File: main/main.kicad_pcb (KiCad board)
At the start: 6 copper layers, 154 parts, among them IC1 TPS54294PWP, IC2 TPS54294PWP, IC3 ESP-PSRAM64H, IC4 PCM1741E, J1 STX-3000, J2 DIN-5_180degree, J3 Barrel_Jack_Switch_Pin3Ring, J4 FPGA_debug, J5 FPGA_GPIO, J6 MCU_debug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

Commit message: Continue PCB layout
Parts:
- moved C66 219.2 mm to (240.8, 88.9), turned to 180 degrees
- moved U5 218.3 mm to (249.4, 91.3)
- moved R41 216.6 mm to (231.0, 88.9), turned to 180 degrees
- moved R40 215.9 mm to (235.7, 86.7)
- moved J1 215.1 mm to (248.4, 78.8)
- moved C67 214.2 mm to (225.2, 88.9), turned to 0 degrees
- moved R42 213.7 mm to (235.7, 88.9), turned to 180 degrees
- moved C68 213.5 mm to (231.0, 86.7), turned to 180 degrees
- moved C64 204.4 mm to (224.2, 80.5)
- moved C65 204.2 mm to (237.3, 80.5)
- moved IC4 204.2 mm to (229.9, 80.5)
- moved C69 199.9 mm to (240.8, 93.9)
- moved J3 193.8 mm to (45.2, 104.0), turned to 270 degrees
- moved C70 181.2 mm to (225.2, 93.8)
- moved C55 156.5 mm to (42.7, 172.8)
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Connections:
- JP2 pad 1: +1V8 -> Net-(C14-Pad1)
- JP2 pad 2: Net-(C14-Pad1) -> +1V8
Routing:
- net /DAC/LINE_OUT_R: track 0.00 -> 48.9 mm
- net Net-(C1-Pad1): track 0.00 -> 47.1 mm
- net /MCU/MIDI_IN: track 76.5 -> 43.8 mm
- net /MCU/FBKey4: track 12.1 -> 42.9 mm
- net /DAC/LINE_OUT_L: track 0.00 -> 30.0 mm, vias 0 -> 2
- net Net-(C65-Pad1): track 0.00 -> 26.5 mm
- net /MCU/FBKey3: track 14.0 -> 37.4 mm
- net Net-(C4-Pad1): track 3.13 -> 26.1 mm
- net Net-(C69-Pad2): track 0.00 -> 23.0 mm
- net Net-(R29-Pad1): track 0.00 -> 22.3 mm
- net /FBKey0: track 18.5 -> 38.4 mm
- net Net-(R28-Pad1): track 0.00 -> 19.4 mm
- net /FBKey2: track 14.7 -> 33.7 mm
- net /FBKey1: track 15.9 -> 34.5 mm
- net Net-(R27-Pad1): track 0.00 -> 16.5 mm
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
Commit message: Continue PCB layout
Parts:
- Backup SPI: renamed from J8
- I2S Breakout: renamed from J9
- moved R36 218.3 mm to (231.1, 31.2)
- moved I2S Breakout 189.7 mm to (229.0, 53.0)
- moved R35 169.4 mm to (206.1, 62.5)
- moved R33 168.6 mm to (206.1, 66.5)
- moved R31 167.8 mm to (206.1, 70.5)
- moved B 166.5 mm to (184.8, 79.8), turned to 0 degrees
- moved A 165.3 mm to (184.8, 75.6), turned to 0 degrees
- moved C 157.2 mm to (184.8, 84.0), turned to 0 degrees
- moved R39 156.4 mm to (191.4, 84.0)
- moved R37 150.6 mm to (191.4, 79.8)
- moved R38 142.0 mm to (191.4, 75.6)
- moved R19 98.6 mm to (291.9, 139.6)
- moved R24 94.4 mm to (288.9, 132.2)
- moved C30 92.7 mm to (286.0, 145.6)
- moved C40 89.9 mm to (283.0, 143.1)
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- renumbered R32 to A, R30 to B, R34 to C
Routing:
- net Net-(R34-Pad2): track 0.00 -> 35.5 mm, vias 0 -> 2
- net /DAC/I2S1: track 0.00 -> 32.0 mm, vias 0 -> 2
- net /DAC/I2S2: track 0.00 -> 28.9 mm
- net /DAC/I2S0: track 0.00 -> 26.0 mm
- net Net-(R32-Pad2): track 0.00 -> 24.0 mm
- net Net-(R30-Pad2): track 0.00 -> 23.9 mm, vias 0 -> 2
- net Net-(J9-Pad3): track 4.16 -> 27.4 mm
- net Net-(J9-Pad2): track 4.16 -> 26.7 mm
- net Net-(J9-Pad1): track 4.18 -> 26.1 mm
- net /DAC/DAC_I2S_LR_SELECT: track 0.00 -> 16.5 mm
- net /DAC/DAC_I2S_DATA: track 0.00 -> 14.3 mm
- net /DAC/DAC_I2S_CLK: track 0.00 -> 13.3 mm
- net Net-(C1-Pad1): track 47.1 -> 52.8 mm
- net Net-(D1-Pad2): track 59.0 -> 63.6 mm
- net Net-(D1-Pad1): track 19.9 -> 24.0 mm
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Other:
- copper layers 6 -> 4
- board text added: "Solder here and cut A, B and C to use breakout I2S"

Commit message: Some more routing
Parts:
- moved C30 127.9 mm to (195.0, 55.6)
- moved C40 126.8 mm to (180.0, 69.2), turned to 270 degrees
- moved C39 120.8 mm to (177.5, 69.2), turned to 270 degrees
- moved C28 118.5 mm to (195.0, 50.7)
- moved C44 115.0 mm to (190.0, 65.5), turned to 180 degrees
- moved C20 112.3 mm to (190.5, 40.0)
- moved C43 112.1 mm to (190.0, 63.4), turned to 180 degrees
- moved C27 108.9 mm to (195.0, 48.2)
- moved C21 107.8 mm to (190.2, 61.1), turned to 180 degrees
- moved C31 105.5 mm to (195.0, 58.1)
- moved C25 105.2 mm to (190.2, 50.8), turned to 180 degrees
- moved C34 103.4 mm to (195.0, 65.5)
- moved C26 100.2 mm to (190.2, 48.2), turned to 180 degrees
- moved C33 99.5 mm to (195.0, 63.0)
- moved C32 98.7 mm to (195.0, 60.6)
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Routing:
- net GND: track 0.00 -> 104.1 mm, vias 0 -> 5
- net +1V0: track 0.00 -> 88.1 mm, vias 0 -> 6
- net +1V8: track 0.00 -> 27.6 mm
- net +3V3: track 0.16 -> 19.9 mm
- net Net-(U2-Pad6): track 0.00 -> 7.87 mm
- added copper zone on In2.Cu, net +3V3
- added copper zone on In1.Cu, net GND
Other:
- board outline added: 292.1 x 177.8 mm

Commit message: PCB getting close to being fully connected
Still missing the power circuit, will look at it tomorrow.
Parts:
- removed A, B, C: 0, Jumper:SolderJumper-2_P1.3mm_Bridged2Bar_RoundedPad1.0x1.5mm
- added R30: 0, Jumper:SolderJumper-2_P1.3mm_Bridged2Bar_RoundedPad1.0x1.5mm, F.Cu at (224.5, 105.3)
- added R32: 0, Jumper:SolderJumper-2_P1.3mm_Bridged2Bar_RoundedPad1.0x1.5mm, F.Cu at (224.5, 101.1)
- added R34: 0, Jumper:SolderJumper-2_P1.3mm_Bridged2Bar_RoundedPad1.0x1.5mm, F.Cu at (224.5, 109.4)
- J8: renamed from Backup SPI
- J9: renamed from I2S Breakout
- moved R24 155.5 mm to (148.8, 64.8), turned to 270 degrees
- moved C48 137.3 mm to (171.4, 44.2), turned to 90 degrees
- moved C52 134.3 mm to (183.8, 44.4), turned to 90 degrees
- moved R23 133.0 mm to (154.9, 58.9), turned to 90 degrees
- moved J8 132.6 mm to (94.8, 21.3), turned to 270 degrees
- moved R21 129.5 mm to (177.4, 29.0), turned to 90 degrees
- moved R22 129.5 mm to (173.9, 29.1), turned to 90 degrees
- moved R25 127.0 mm to (152.9, 64.8), turned to 270 degrees
- moved C49 126.5 mm to (174.7, 44.4), turned to 90 degrees
- moved R19 123.1 mm to (179.8, 88.8)
- moved C51 122.6 mm to (180.7, 44.4), turned to 90 degrees
- moved C50 114.4 mm to (177.7, 44.4), turned to 90 degrees
- moved C53 112.2 mm to (186.8, 44.4), turned to 90 degrees
- moved C47 111.2 mm to (167.9, 44.2), turned to 90 degrees
- moved C46 100.2 mm to (173.1, 38.0), turned to 90 degrees
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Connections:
- J5 pad 1: /FPGA/GPIO0 -> +3V3
- J5 pad 10: /FPGA/GPIO5 -> /FPGA/GPIO4
- J5 pad 2: /FPGA/GPIO9 -> GND
- J5 pad 3: /FPGA/GPIO1 -> /FPGA/GPIO0
- J5 pad 4: /FPGA/GPIO8 -> /FPGA/GPIO7
- J5 pad 5: /FPGA/GPIO2 -> /FPGA/GPIO1
- J5 pad 6: /FPGA/GPIO7 -> /FPGA/GPIO6
- J5 pad 7: /FPGA/GPIO3 -> /FPGA/GPIO2
- J5 pad 8: /FPGA/GPIO6 -> /FPGA/GPIO5
- J5 pad 9: /FPGA/GPIO4 -> /FPGA/GPIO3
- L2 pad 1: Net-(C14-Pad1) -> Net-(C12-Pad2)
- L2 pad 2: Net-(C12-Pad2) -> Net-(C14-Pad1)
- U3 pad P8: /FPGA/GPIO9 -> Net-(U3-PadP8)
- U3 pad R5: /FPGA/GPIO3 -> /FPGA/GPIO0
- U3 pad R6: /FPGA/GPIO1 -> /FPGA/GPIO7
- U3 pad R7: /FPGA/GPIO0 -> Net-(U3-PadR7)
- U3 pad R8: /FPGA/GPIO8 -> Net-(U3-PadR8)
- U3 pad T12: Net-(U3-PadT12) -> /FPGA/GPIO3
- U3 pad T5: /FPGA/GPIO2 -> /FPGA/GPIO6
- U3 pad T7: /FPGA/GPIO7 -> /FPGA/GPIO1
- U3 pad T8: /FPGA/GPIO6 -> /FPGA/GPIO5
- U3 pad T9: /FPGA/GPIO5 -> /FPGA/GPIO2
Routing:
- net GND: track 104.1 -> 329.8 mm, vias 5 -> 26
- net +3V3: track 19.9 -> 184.2 mm, vias 0 -> 13
- net /MCU/~RESET: track 0.00 -> 96.6 mm, vias 0 -> 1
- net /MCU/BACKUP_SPI_CLK: track 0.00 -> 93.8 mm, vias 0 -> 1
- net /MCU/BACKUP_SPI_MISO: track 0.00 -> 93.4 mm, vias 0 -> 1
- net /MCU/BACKUP_SPI_MOSI: track 0.00 -> 93.3 mm, vias 0 -> 1
- net /MCU/BACKUP_SPI_CS: track 0.00 -> 92.6 mm, vias 0 -> 1
- net /MCU/GPIO9: track 0.00 -> 91.2 mm, vias 0 -> 2
- net /MCU/GPIO8: track 0.00 -> 85.5 mm, vias 0 -> 2
- net /MCU/GPIO7: track 0.00 -> 75.7 mm
- net /MCU/GPIO0: track 0.00 -> 74.9 mm
- net /MCU/GPIO1: track 0.00 -> 71.3 mm
- net /MCU/GPIO6: track 0.00 -> 70.8 mm
- net /MCU/DBG_SWDIOTMS: track 0.00 -> 70.0 mm, vias 0 -> 1
- net /MCU/GPIO2: track 0.00 -> 69.2 mm
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
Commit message: Almost finished with PCB layout
- Fixed FPGA power layout. The 1V0, 1V8 and 3V3 pins have to be
  connected to vias which in turn connect to fat lanes

- Added logo and names

- Started power circuit, this needs some work
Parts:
- added logo: G***, logo:logo, F.Cu at (72.8, 97.2)
- added svg2mod: G***, logo:logo, F.Cu at (207.0, 67.6)
- moved C6 200.4 mm to (213.5, 58.6), turned to 90 degrees
- moved R13 188.6 mm to (205.0, 55.1), turned to 180 degrees
- moved L3 188.5 mm to (208.4, 99.6), turned to 270 degrees
- moved C14 183.4 mm to (205.0, 58.7), turned to 180 degrees
- moved C15 178.1 mm to (205.0, 62.3), turned to 180 degrees
- moved L2 175.8 mm to (208.4, 62.5), turned to 90 degrees
- moved J3 175.7 mm to (217.0, 67.4), turned to 90 degrees
- moved C8 174.3 mm to (206.5, 67.2), turned to 180 degrees
- moved C9 170.1 mm to (206.5, 70.5), turned to 180 degrees
- moved R16 168.7 mm to (200.2, 55.1), turned to 180 degrees
- moved C12 164.9 mm to (205.8, 74.8), turned to 90 degrees
- moved C13 164.7 mm to (205.8, 87.3), turned to 270 degrees
- moved C11 164.5 mm to (206.5, 95.0), turned to 180 degrees
- moved C16 164.4 mm to (205.2, 100.0), turned to 180 degrees
- moved C17 164.4 mm to (205.2, 103.5), turned to 180 degrees
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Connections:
- net Net-(C1-Pad1) renamed /Power Supply/POWER_IN
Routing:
- net +3V3: track 184.2 -> 403.0 mm, vias 13 -> 24
- net /DAC/DAC_MODE_LATCH: track 0.00 -> 113.2 mm, vias 0 -> 2
- net /DAC/DAC_MODE_DATA: track 0.00 -> 110.0 mm, vias 0 -> 2
- net /DAC/DAC_MODE_CTRL_CLK: track 0.00 -> 109.7 mm, vias 0 -> 2
- net /FPGA/MCU_CLOCK_IN: track 4.04 -> 85.4 mm, vias 0 -> 2
- net +3.3VA: track 0.00 -> 75.6 mm
- net /DAC/DAC_SYS_CLK: track 1.03 -> 76.4 mm, vias 0 -> 2
- net Net-(C14-Pad1): track 12.7 -> 84.7 mm
- net /DAC/I2S0: track 1.06 -> 53.7 mm, vias 0 -> 2
- net /DAC/I2S2: track 7.18 -> 59.3 mm, vias 0 -> 2
- net /DAC/I2S1: track 1.12 -> 51.5 mm, vias 0 -> 2
- net /FBKey0: track 38.4 -> 83.3 mm
- net GND: track 329.8 -> 373.4 mm, vias 26 -> 94
- net /MCU/FPGA_PROGRAM_B: track 7.34 -> 49.7 mm, vias 0 -> 2
- net /FPGA/DONE: track 10.8 -> 52.4 mm, vias 0 -> 2
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- added copper zone on F.Cu, net /Power Supply/POWER_IN
- added copper zone on F.Cu, net GND
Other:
- board size 292.1 x 177.8 mm -> 166.6 x 111.3 mm
- net class Default: clearance 0.2 -> 0.15; via_dia 0.8 -> 0.6; via_drill 0.4 -> 0.3
- net class Power added: clearance 0.15, trace_width 0.6, via_dia 0.6, via_drill 0.3
- rule trace_clearance: 0.2 -> 0.15
- board text added: "Andreas Klavenes Berg Eivind Kløvjan Halvor Bjørstad Iver Håkonsen Lars Murud Aurud Magnus Alexander Krumbacher Oskar Sveinsen"

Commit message: Finished (?) board
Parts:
- moved D2 50.2 mm to (184.6, 146.6)
- moved FB1 50.2 mm to (176.1, 151.3)
- moved R11 50.2 mm to (176.1, 146.6)
- moved R12 50.2 mm to (184.8, 151.3)
- moved R10 39.2 mm to (210.0, 85.5), turned to 180 degrees
- moved R17 33.9 mm to (192.6, 86.7), turned to 270 degrees
- moved JP3 15.0 mm to (184.5, 121.7), turned to 180 degrees
- moved JP1 5.37 mm to (184.5, 107.3), turned to 180 degrees
- moved JP2 4.82 mm to (184.5, 114.5), turned to 180 degrees
- moved C20 1.70 mm to (178.9, 69.4)
- moved C42 1.70 mm to (181.0, 75.0)
- moved C18 0.56 mm to (199.7, 87.7)
- moved C43 0.45 mm to (179.0, 95.0)
- moved C44 0.45 mm to (179.0, 97.1)
- moved R15 0.19 mm to (200.1, 107.2)
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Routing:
- net +1V0: track 126.6 -> 51.1 mm
- net +1V8: track 76.7 -> 57.8 mm
- net +3V3: track 403.0 -> 385.8 mm, vias 24 -> 25
- net +3.3VA: track 75.6 -> 90.6 mm
- net Net-(C16-Pad1): track 24.4 -> 38.5 mm
- net Net-(C18-Pad1): track 0.00 -> 12.1 mm, vias 0 -> 2
- net Net-(J9-Pad1): track 34.3 -> 22.6 mm
- net Net-(C14-Pad1): track 84.7 -> 96.0 mm
- net Net-(IC2-Pad12): track 17.5 -> 28.0 mm, vias 2 -> 3
- net Net-(C7-Pad1): track 3.37 -> 11.4 mm, vias 0 -> 2
- net Net-(J9-Pad2): track 29.5 -> 23.1 mm
- net Net-(C4-Pad1): track 61.5 -> 55.5 mm
- net Net-(IC1-Pad11): track 29.1 -> 34.2 mm
- net GND: track 373.4 -> 368.5 mm, vias 94 -> 95
- net Net-(J9-Pad3): track 24.9 -> 23.7 mm
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- added copper zone on F.Cu, net +1V0
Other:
- board size 166.6 x 111.3 mm -> 166 x 112 mm
- board text added: "Debug"
- board text added: "FPGA"
- board text added: "GPIO"
- board text added: "MCU"
- board text added: "SPI"
- board text removed: "Solder here and cut A, B and C to use breakout I2S"

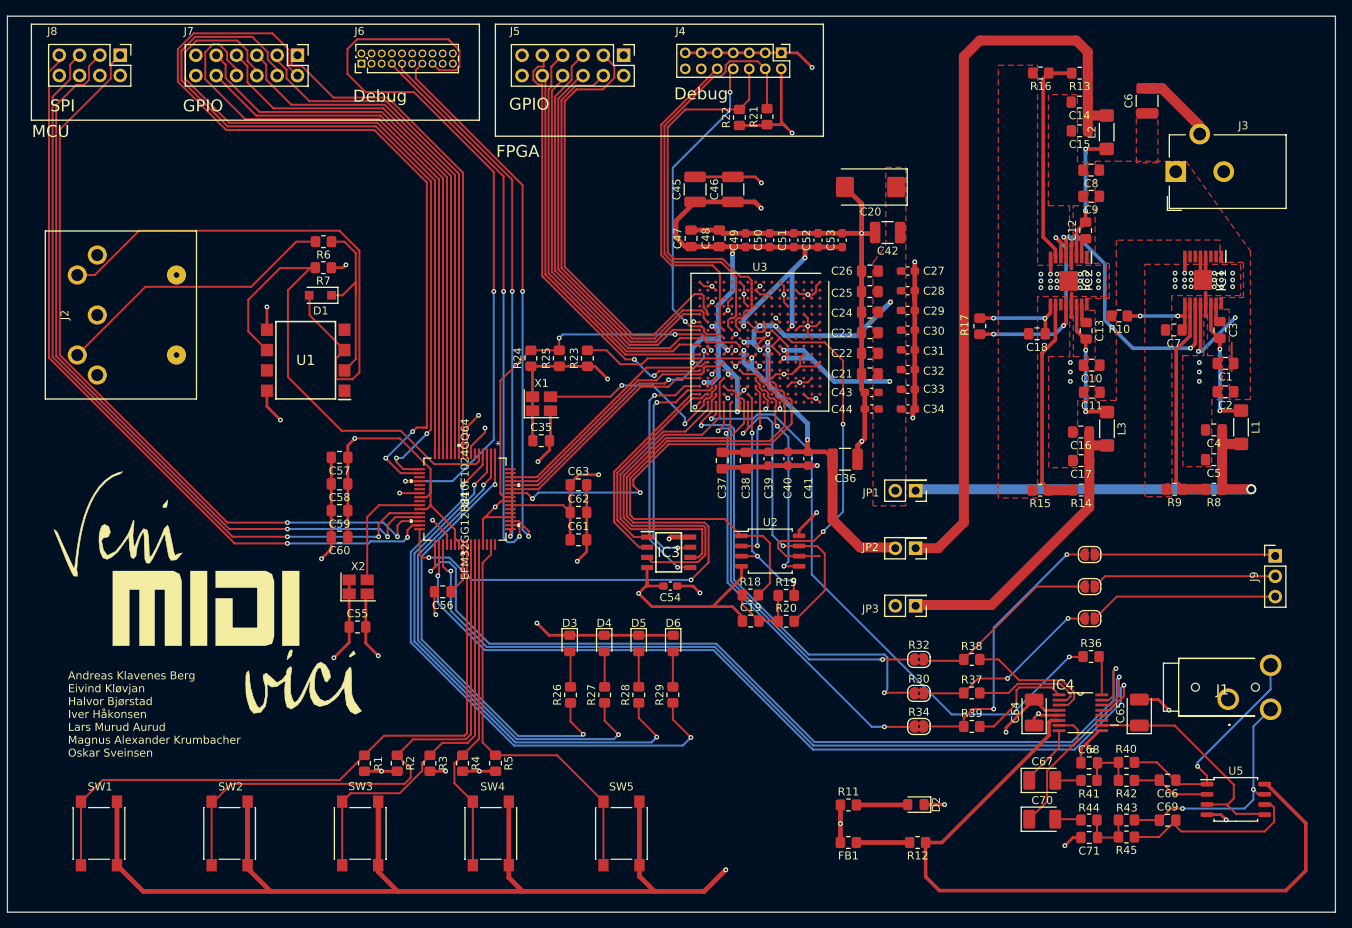
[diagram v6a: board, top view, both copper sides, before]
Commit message: Fixes after review
- +1V0 and +1V8 power zones on the backside of the FPGA
- Vias directly next to decoupling capacitors
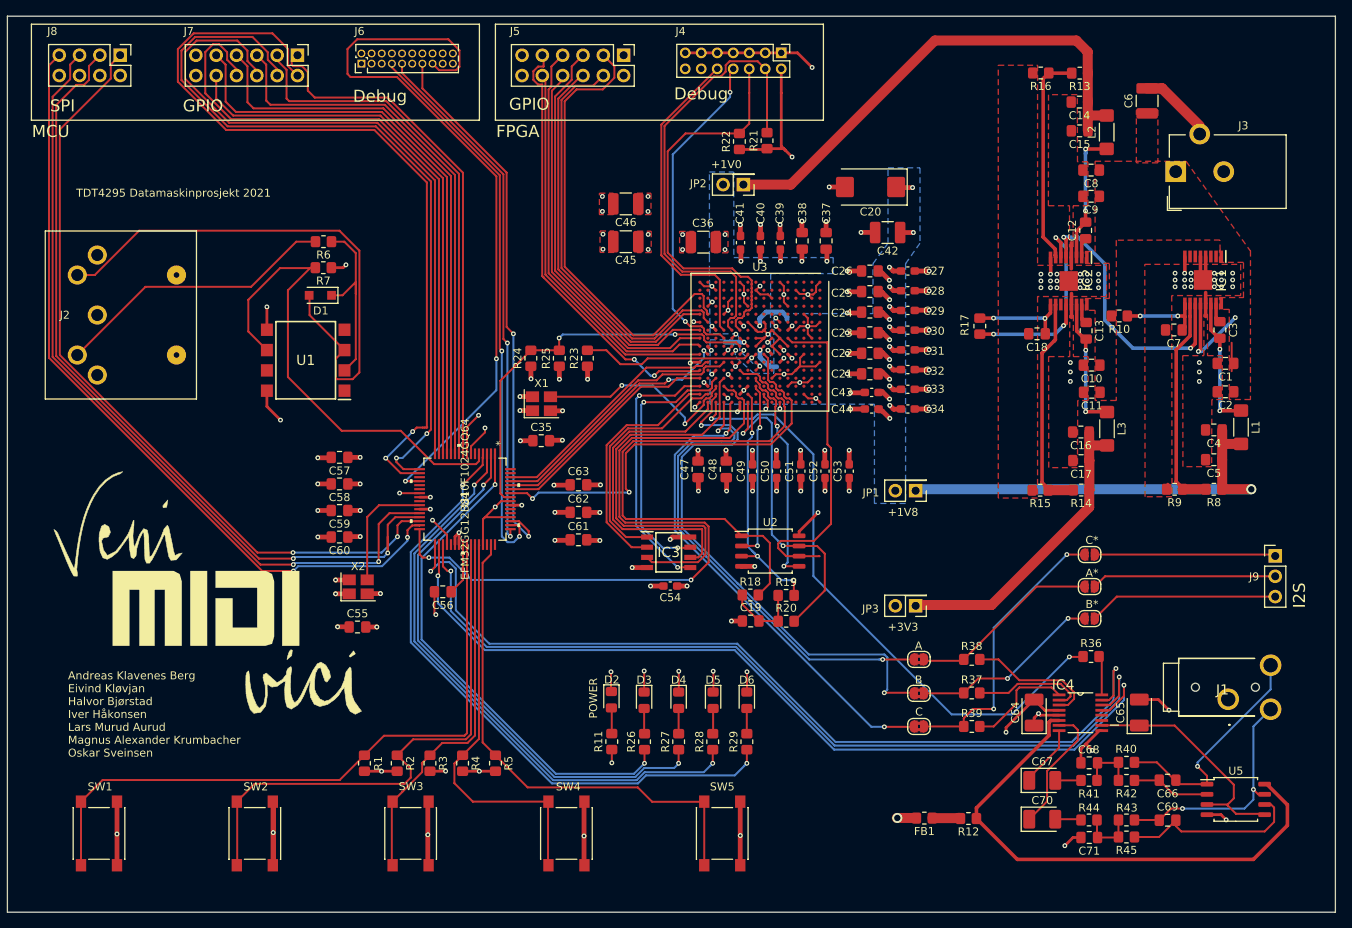
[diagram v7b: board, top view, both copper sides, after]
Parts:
- moved JP2 50.3 mm to (163.0, 69.0)
- moved D2 40.3 mm to (146.5, 133.4), turned to 270 degrees
- moved C36 32.4 mm to (158.0, 76.2), turned to 180 degrees
- moved R11 30.6 mm to (146.5, 138.7), turned to 90 degrees
- moved C37 30.4 mm to (173.3, 76.1), turned to 90 degrees
- moved C47 28.9 mm to (157.3, 104.6)
- moved C48 28.9 mm to (160.9, 104.6)
- moved C49 28.9 mm to (164.1, 104.9)
- moved C50 28.9 mm to (167.2, 104.9)
- moved C51 28.9 mm to (170.2, 104.9)
- moved C52 28.9 mm to (173.2, 104.9)
- moved C53 28.9 mm to (176.2, 104.9)
- moved C38 28.3 mm to (170.4, 76.1), turned to 90 degrees
- moved C41 28.3 mm to (162.6, 76.3), turned to 90 degrees
- moved C40 27.2 mm to (165.1, 76.3), turned to 90 degrees
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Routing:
- net +3V3: track 385.8 -> 145.5 mm, vias 25 -> 54
- net GND: track 368.5 -> 272.2 mm, vias 95 -> 138
- net +1V8: track 57.8 -> 11.0 mm, vias 5 -> 11
- net Net-(C14-Pad1): track 96.0 -> 63.6 mm
- net +3.3VA: track 90.6 -> 66.4 mm
- net /MCU/FBKey4: track 51.3 -> 63.9 mm
- net /MCU/FBKey3: track 42.4 -> 51.9 mm
- net /DAC/I2S2: track 59.3 -> 68.0 mm
- net /DAC/I2S1: track 51.5 -> 60.1 mm
- net /DAC/I2S0: track 53.7 -> 61.2 mm
- net Net-(R26-Pad1): track 57.0 -> 64.1 mm
- net Net-(R27-Pad1): track 62.2 -> 69.2 mm
- net /FBKey2: track 52.5 -> 46.3 mm
- net Net-(R28-Pad1): track 68.1 -> 74.3 mm
- net Net-(R29-Pad1): track 73.3 -> 79.4 mm
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- added copper zone on B.Cu, net +1V0
- added copper zone on B.Cu, net +1V8
- added copper zone on F.Cu, net +1V8
- added copper zone on F.Cu, net +3V3
- removed copper zone on F.Cu, net +1V0
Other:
- board text added: "+1V0"
- board text added: "+1V8"
- board text added: "+3V3"
- board text added: "0"
- board text added: "1"
- board text added: "2"
- board text added: "3"
- board text added: "4"
- board text added: "5"
- board text added: "6"
- board text added: "7"
- board text added: "8"
- board text added: "9"
- board text added: "A"
- board text added: "A*"
- board text added: "B"
- board text added: "B*"
- board text added: "C"
- board text added: "C*"
- board text added: "CLK"
- board text added: "CS"
- board text added: "DATA"
- board text added: "GND"
- board text added: "I2S"
- board text added: "LR_SELECT"
- board text added: "MISO"
- board text added: "MOSI"
- board text added: "POWER"
- board text added: "TDT4295 Datamaskinprosjekt 2021"
